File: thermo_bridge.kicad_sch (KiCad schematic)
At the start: 4 parts

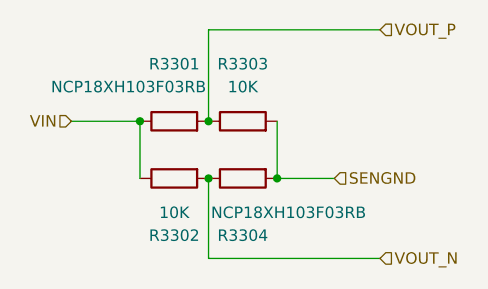
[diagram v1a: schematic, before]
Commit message: Increase layout size to accommodate more SMA connector
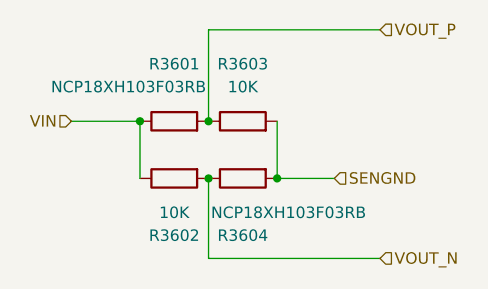
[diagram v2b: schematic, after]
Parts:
- renumbered R3301 to R3601, R3302 to R3602, R3303 to R3603, R3304 to R3604
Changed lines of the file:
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@@
 		(on_board yes)
 		(dnp no)
-		(property "Reference" "R3302"
+		(property "Reference" "R3602"
 			(at 90.17 100.33 90)
 			(effects
@@
 		(on_board yes)
 		(dnp no)
-		(property "Reference" "R3301"
+		(property "Reference" "R3601"
 			(at 90.17 81.28 90)
 			(effects
@@
 		(dnp no)
 		(fields_autoplaced yes)
-		(property "Reference" "R3303"
+		(property "Reference" "R3603"
 			(at 97.79 81.28 90)
 			(effects
@@
 		(on_board yes)
 		(dnp no)
-		(property "Reference" "R3304"
+		(property "Reference" "R3604"
 			(at 97.79 100.33 90)
 			(effects
